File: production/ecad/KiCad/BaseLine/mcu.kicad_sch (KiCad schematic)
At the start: 0 parts

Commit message: worked on MCU
input all symbols and started circuitry
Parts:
- added C12, C13: 100nF, symbol Device:C
- added J6: 1332645, 1332645:PHOENIX_1332645, symbol 1332645:1332645
- added R12, R13: 5.1k, symbol Device:R_Small_US
- added R18, R19: 0, symbol Device:R_Small_US
- added R20: 22.1k, symbol Device:R_Small_US
- added R21: 47.5k, symbol Device:R_Small_US
- added R22: 10k, symbol Device:R_Small_US
- added U4: ESP32-WROOM-32UE_M113EH6400UH3Q0_, ESP32-WROOM-32UE_M113EH6400UH3Q0_:MODULE_ESP32-WROOM-32UE_M113EH6400UH3Q0_, symbol ESP32-WROOM-32UE_M113EH6400UH3Q0_:ESP32-WROOM-32UE_M113EH6400UH3Q0_
- added U5: CP2102N-A02-GQFN28, CP2102N-A02-GQFN28:QFN50P500X500X80-29N, symbol CP2102N-A02-GQFN28:CP2102N-A02-GQFN28
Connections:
- new net: J6.A5 (CC1), R12.1
- new net: R20.2, R21.1, U5.8 (VBUS)
- new net: J6.B5 (CC2), R13.1
- new net: R19.2, U5.25 (RXD)
- new net: R18.2, U5.26 (TXD)
- new net: R22.2, U5.9 (~{RST})
- new net: U4.1 (GND), U4.15 (GND), U4.38 (GND), U4.39_1 (GND), U4.39_10 (GND), U4.39_11 (GND), U4.39_12 (GND), U4.39_13 (GND), U4.39_14 (GND), U4.39_15 (GND), U4.39_16 (GND), U4.39_17 (GND), U4.39_18 (GND), U4.39_19 (GND), U4.39_2 (GND), U4.39_20 (GND), U4.39_21 (GND), U4.39_3 (GND), U4.39_4 (GND), U4.39_5 (GND), U4.39_6 (GND), U4.39_7 (GND), U4.39_8 (GND), U4.39_9 (GND)
- new net: U4.17 (NC), U4.18 (NC), U4.19 (NC), U4.20 (NC), U4.21 (NC), U4.22 (NC)
- new net +3.3V: C12.1, C13.1, R22.1, U5.6 (VDD), U5.7 (VREGIN)
- new net DTR: U5.28 (DTR)
- new net GND: C12.2, C13.2, J6.A1_B12 (GND_A), J6.B1_A12 (GND_B), J6.SH1 (SHIELD), J6.SH2 (SHIELD__1), J6.SH3 (SHIELD__2), J6.SH4 (SHIELD__3), R12.2, R13.2, R21.2, U5.29 (GND__1), U5.3 (GND)
- new net RTS: U5.24 (RTS)
- new net UART_RXD: R19.1
- new net UART_TXD: R18.1
- new net USB_D+: J6.A6 (DP1), J6.B6 (DP2), U5.4 (D+)
- new net USB_D-: J6.A7 (DN1), J6.B7 (DN2), U5.5 (D-)
- new net VBUS: J6.A4_B9 (VBUS_A), J6.B4_A9 (VBUS_B), R20.1
- no-connect marks 0 -> 14

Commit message: more MCU stuff
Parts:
- added C14: 0.1uF, symbol Device:C
- added C15: 10uF, symbol Device:C
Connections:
- net +3.3V: now also U4.2 (3V3), C14.1, C15.1
- net GND: now also U4.1 (GND), U4.15 (GND), U4.38 (GND), U4.39_1 (GND), U4.39_10 (GND), U4.39_11 (GND), U4.39_12 (GND), U4.39_13 (GND), U4.39_14 (GND), U4.39_15 (GND), U4.39_16 (GND), U4.39_17 (GND), U4.39_18 (GND), U4.39_19 (GND), U4.39_2 (GND), U4.39_20 (GND), U4.39_21 (GND), U4.39_3 (GND), U4.39_4 (GND), U4.39_5 (GND), U4.39_6 (GND), U4.39_7 (GND), U4.39_8 (GND), U4.39_9 (GND), C14.2, C15.2
- net UART_RXD: now also U4.35 (TXD0)
- net UART_TXD: now also U4.34 (RXD0)
- net IO0: now reaches U4.25 (IO0)
- net EN: now reaches U4.3 (EN)
- no-connect marks 14 -> 16

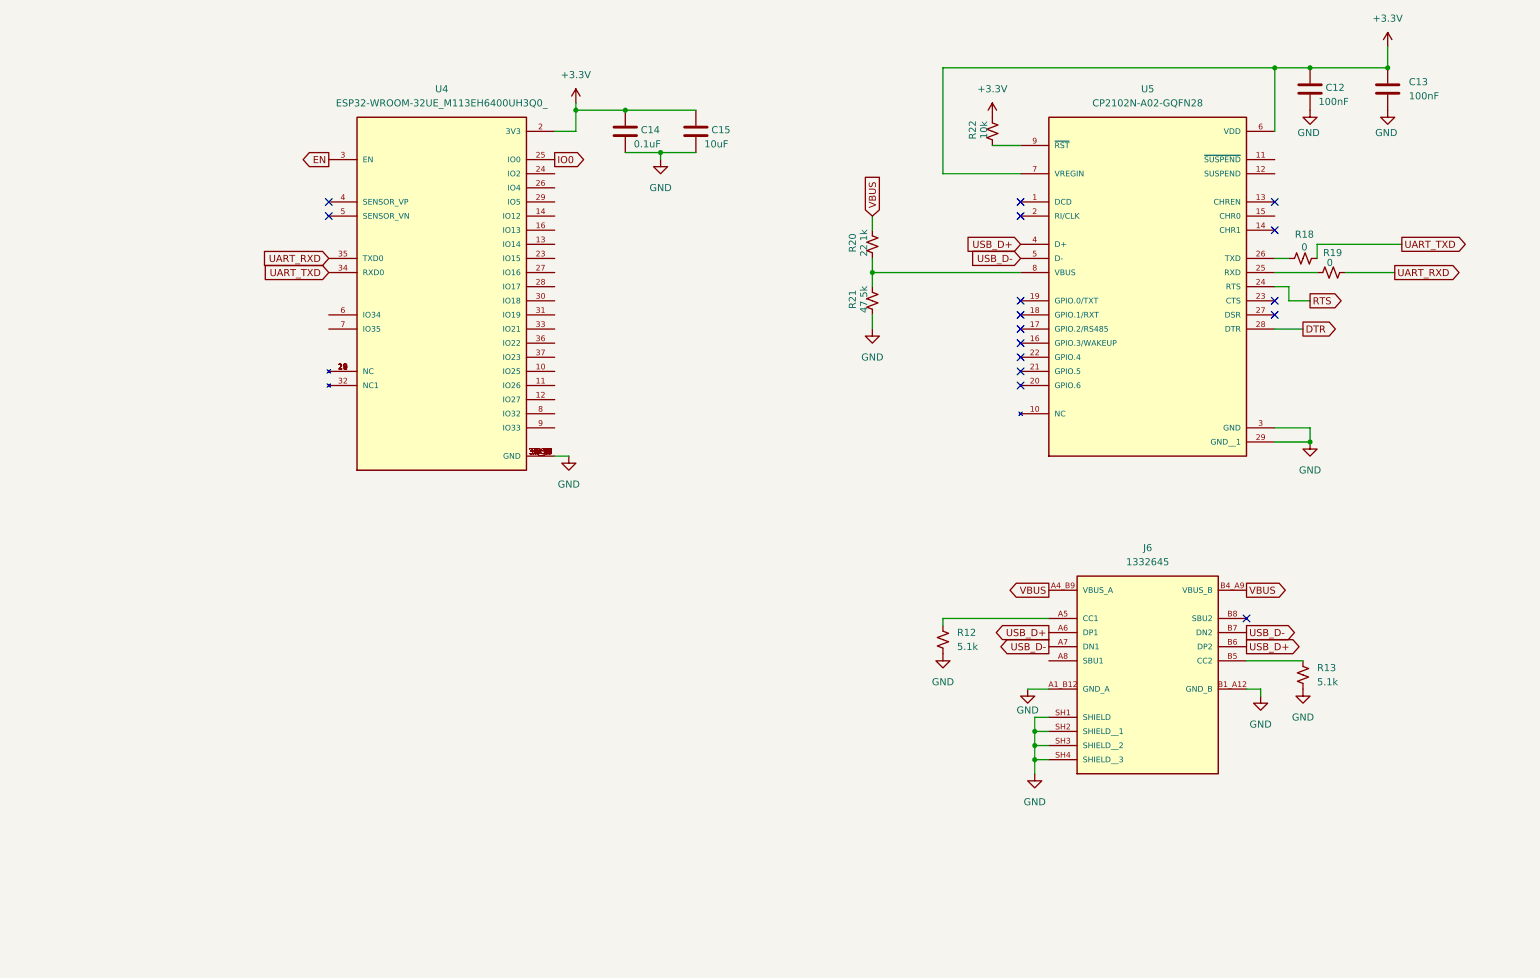
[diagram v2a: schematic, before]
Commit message: organizing MCU
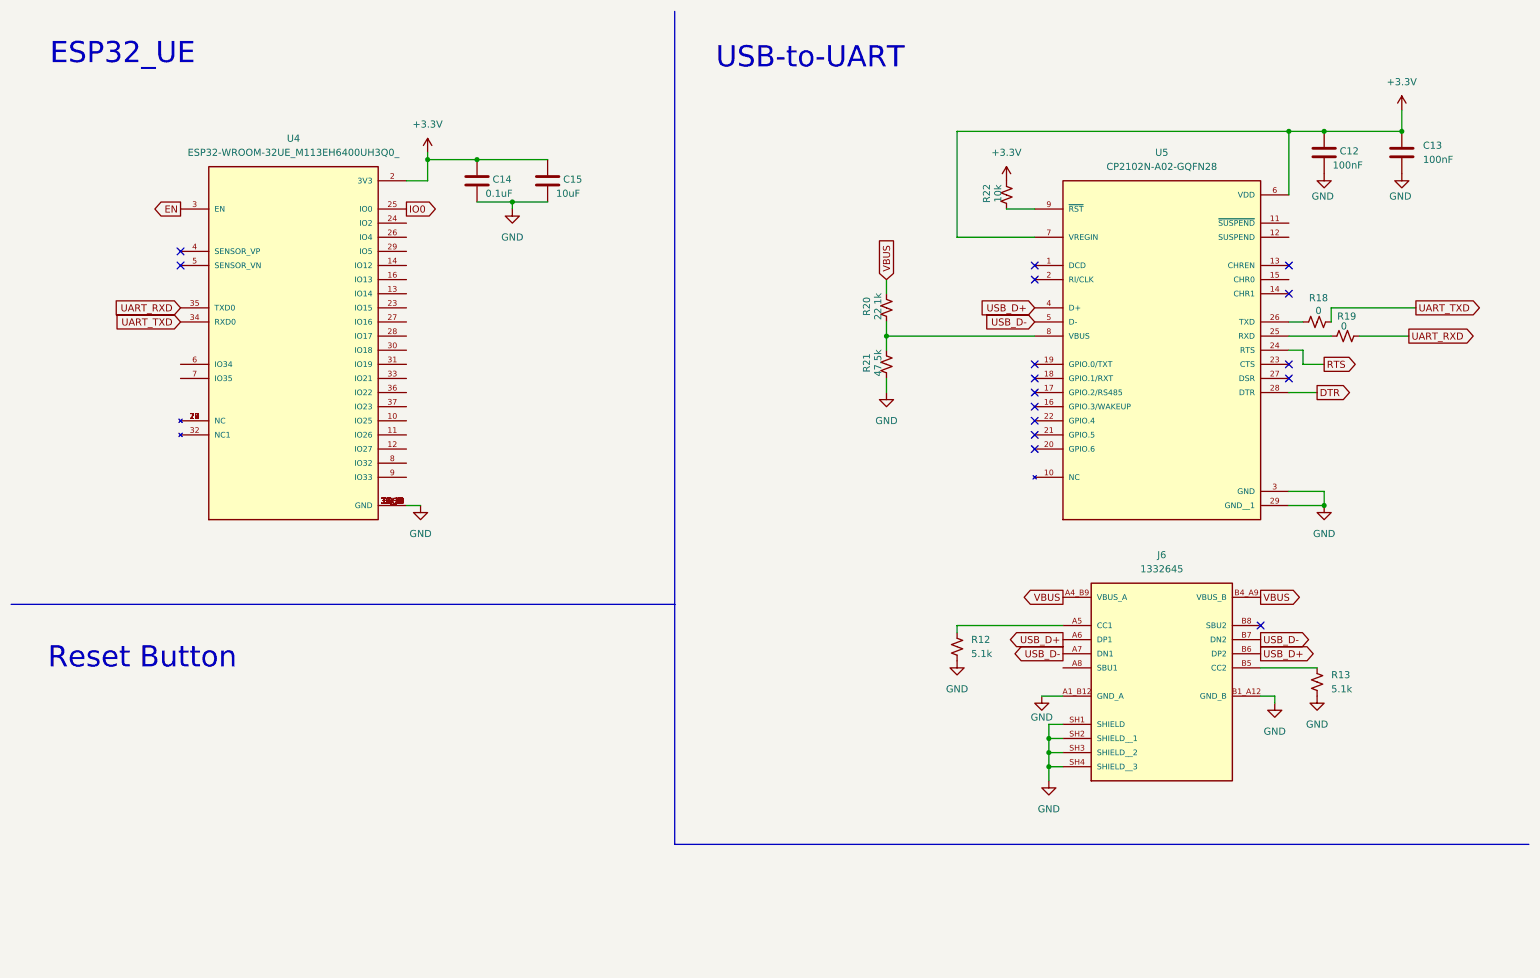
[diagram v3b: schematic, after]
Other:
- note added: "ESP32_UE"
- note added: "Reset Button"
- note added: "USB-to-UART"
- moved on the sheet: C12, C13, C14, C15, J6, R12, R13, R18, R19, R20, R21, R22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

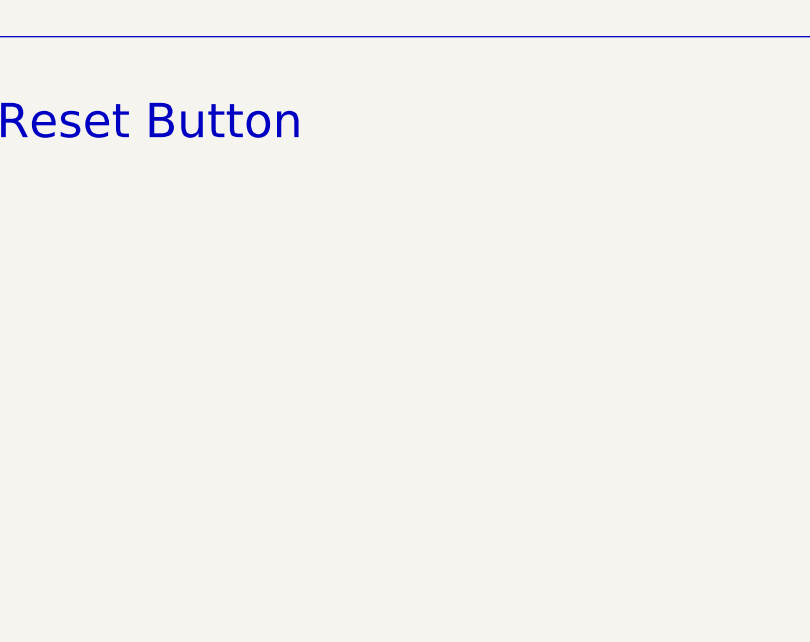
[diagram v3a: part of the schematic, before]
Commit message: Just added push button and something to make sure the 3.3V line doesn't drop for MCU line.
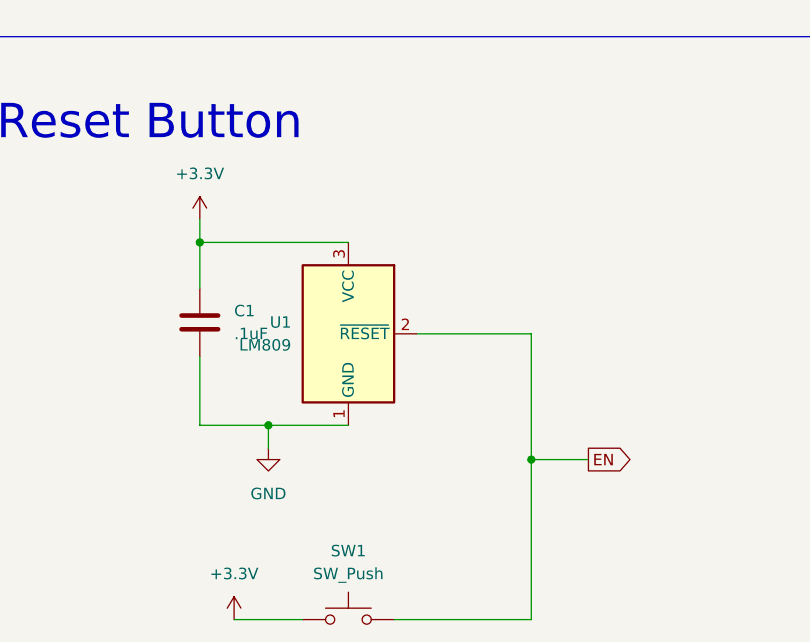
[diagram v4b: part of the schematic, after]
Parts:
- added C1: .1uF, symbol Device:C
- added SW1: SW_Push, symbol Switch:SW_Push
- added U1: LM809, Package_TO_SOT_SMD:SOT-23, symbol Power_Supervisor:LM809
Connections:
- net +3.3V: now also C1.1, SW1.1, U1.3 (VCC)
- net EN: now also SW1.2, U1.2 (~{RESET})
- net GND: now also C1.2, U1.1 (GND)

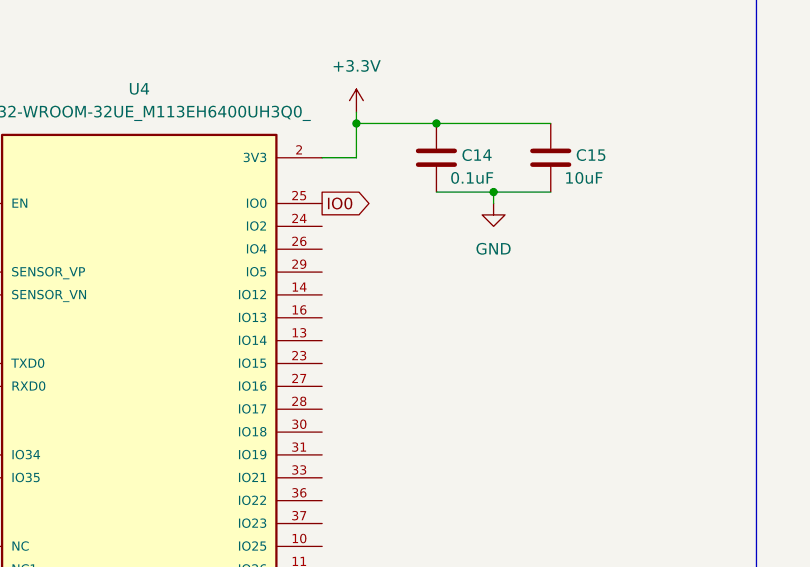
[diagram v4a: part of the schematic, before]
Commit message: Added some connections onto MCU schematic
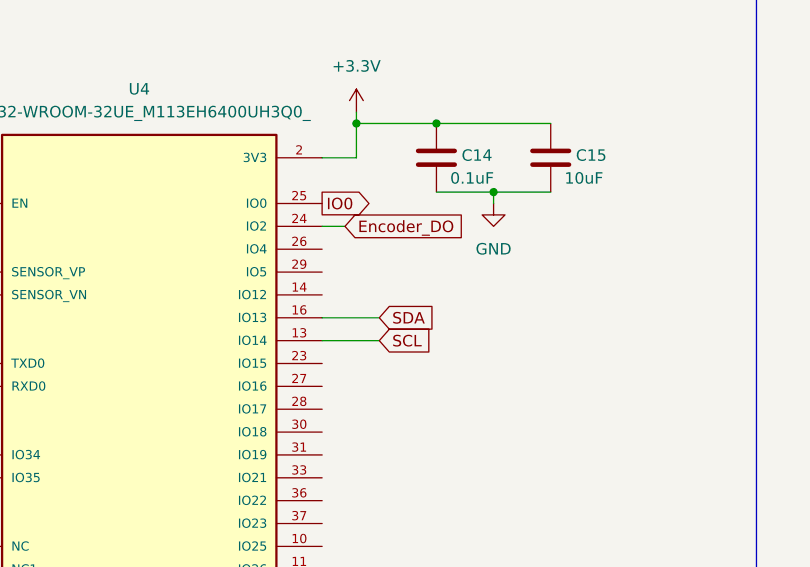
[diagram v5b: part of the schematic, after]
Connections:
- net SCL: now reaches U4.13 (IO14)
- net SDA: now reaches U4.16 (IO13)
- net Encoder_DO: now reaches U4.24 (IO2)
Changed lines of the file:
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@@
+	(wire
+		(pts
+			(xy 82.55 60.96) (xy 88.9 60.96)
+		)
+		(stroke
+			(width 0)
+			(type default)
+		)
+	)
+	(wire
+		(pts
+			(xy 82.55 50.8) (xy 85.09 50.8)
+		)
+		(stroke
+			(width 0)
+			(type default)
+		)
+	)
 	(wire
 		(pts
@@
 			(type default)
 			(color 0 0 0 1)
+		)
+	)
+	(wire
+		(pts
+			(xy 82.55 63.5) (xy 88.9 63.5)
+		)
+		(stroke
+			(width 0)
+			(type default)
 		)
 	)
@@
 		)
 	)
+	(global_label "Encoder_DO"
+		(shape input)
+		(at 85.09 50.8 0)
+		(fields_autoplaced yes)
+		(effects
+			(font
+				(size 1.27 1.27)
+			)
+			(justify left)
+		)
+		(property "Intersheetrefs" "${INTERSHEET_REFS}"
+			(at 99.2027 50.8 0)
+			(effects
+				(font
+					(size 1.27 1.27)
+				)
+				(justify left)
+				(hide yes)
+			)
+		)
+	)
 	(global_label "IO0"
 		(shape output)
@@
 		)
 	)
+	(global_label "SDA"
+		(shape input)
+		(at 88.9 60.96 0)
+		(fields_autoplaced yes)
+		(effects
+			(font
+				(size 1.27 1.27)
+			)
+			(justify left)
+		)
+		(property "Intersheetrefs" "${INTERSHEET_REFS}"
+			(at 95.4533 60.96 0)
+			(effects
+				(font
+					(size 1.27 1.27)
+				)
+				(justify left)
+				(hide yes)
+			)
+		)
+	)
 	(global_label "UART_TXD"
 		(shape output)
@@
 			(effects
 				(font
+					(size 1.27 1.27)
+				)
+				(justify left)
+				(hide yes)
+			)
+		)
+	)
+	(global_label "SCL"
+		(shape input)
+		(at 88.9 63.5 0)
+		(fields_autoplaced yes)
+		(effects
+			(font
+				(size 1.27 1.27)
+			)
+			(justify left)
+		)
+		(property "Intersheetrefs" "${INTERSHEET_REFS}"
+			(at 95.3928 63.5 0)
+			(effects
+				(font
